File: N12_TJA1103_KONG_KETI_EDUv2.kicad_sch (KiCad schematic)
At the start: 65 parts, among them IC1 TJA1103AHN, J1 Conn_02x02_Odd_Even, J2 Conn_02x11_Odd_Even, J3 9-2304372-9, J4 E6S20A-40MT5-Z, Q1 FDN340P, Q2 BSS138, SW2 SW-DIP-ANGLED DS03-254-02BE, Y1 Crystal_GND24_Small

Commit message: fix: add E6S20A component library to assignment
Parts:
- J4: footprint YK_Footprint_LIB:E6S20A40MT5Z -> E6S20A:E6S20A40MT5Z
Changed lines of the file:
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@@
 			)
 		)
-		(property "Footprint" "YK_Footprint_LIB:E6S20A40MT5Z"
+		(property "Footprint" "E6S20A:E6S20A40MT5Z"
 			(at 154.94 191.44 0)
 			(effects

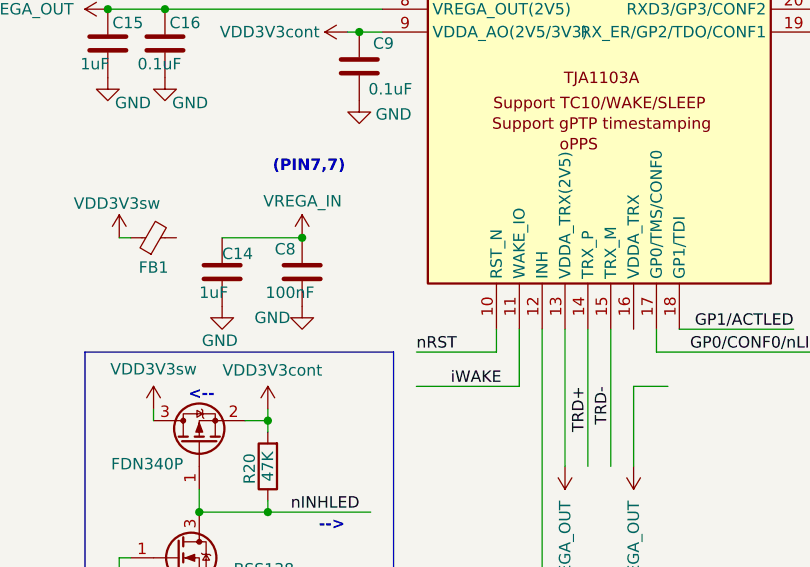
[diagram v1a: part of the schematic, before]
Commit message: fix: connect missing regulator and PHY supply pins
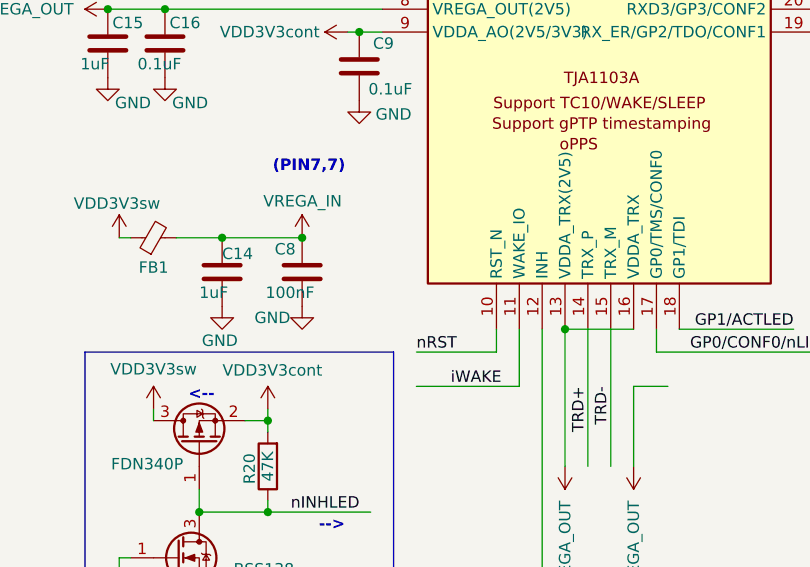
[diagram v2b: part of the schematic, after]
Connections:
- net VREGA_IN: now also FB1.2
- net VREGA_OUT: now also IC1.16 (VDDA_TRX)
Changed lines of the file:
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@@
 		)
+	)
+	(wire
+		(pts
+			(xy 29.21 92.71) (xy 34.29 92.71)
+		)
+		(stroke
+			(width 0)
+			(type default)
+		)
+	)
+	(junction
+		(at 34.29 92.71)
+		(diameter 0)
+		(color 0 0 0 0)
+	)
+	(wire
+		(pts
+			(xy 72.39 102.87) (xy 80.01 102.87)
+		)
+		(stroke
+			(width 0)
+			(type default)
+		)
+	)
+	(junction
+		(at 72.39 102.87)
+		(diameter 0)
+		(color 0 0 0 0)
 	)
 	(sheet_instances

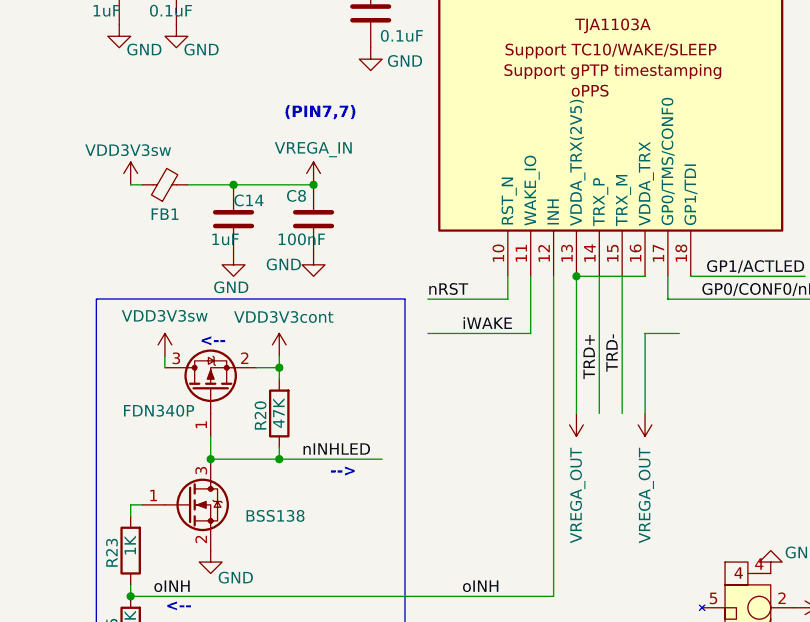
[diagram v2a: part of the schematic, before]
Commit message: fix: mark regulator rails as powered nets
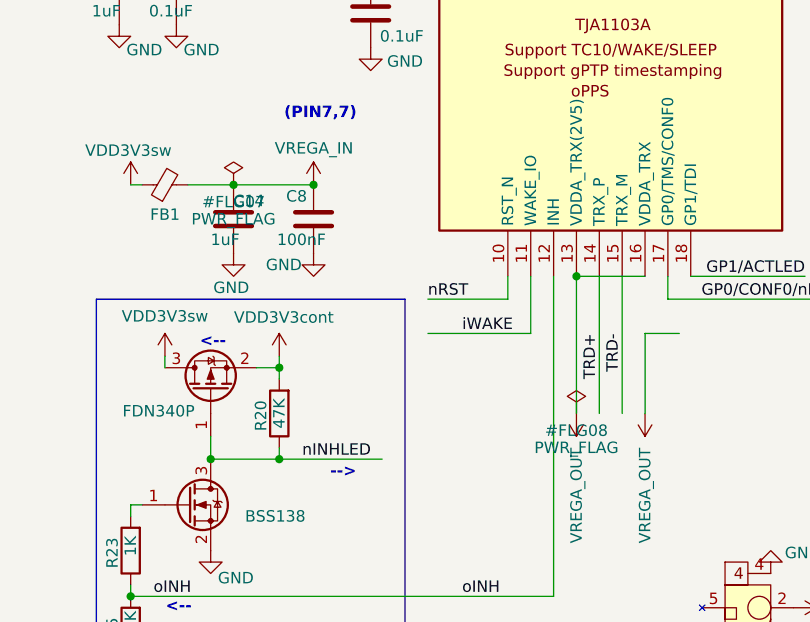
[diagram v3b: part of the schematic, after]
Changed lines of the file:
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@@
 		(color 0 0 0 0)
 	)
-	(sheet_instances
+    (symbol (lib_id "power:PWR_FLAG") (at 72.39 118.11 0) (unit 1)
+    (body_style 1) (exclude_from_sim no) (in_bom yes) (on_board yes) (in_pos_files yes) (dnp no)
+    (property "Reference" "#FLG08"
+      (at 72.39 120.015 0)
+      (show_name no)
+      (do_not_autoplace no)
+      (effects
+					(font
+						(size 1.27 1.27)
+					)
+				)
+    )
+    (property "Value" "PWR_FLAG"
+      (at 72.39 121.92 0)
+      (show_name no)
+      (do_not_autoplace no)
+      (effects
+					(font
+						(size 1.27 1.27)
+					)
+				)
+    )
+    (property "Footprint" ""
+      (at 72.39 118.11 0)
+      (hide yes)
+      (show_name no)
+      (do_not_autoplace no)
+      (effects
+					(font
+						(size 1.27 1.27)
+					)
+				)
+    )
+    (property "Datasheet" ""
+      (at 72.39 118.11 0)
+      (hide yes)
+      (show_name no)
+      (do_not_autoplace no)
+      (effects
+					(font
+						(size 1.27 1.27)
+					)
+				)
+    )
+    (property "Description" "Special symbol for telling ERC where power comes from"
+      (at 72.39 118.11 0)
+      (hide yes)
+      (show_name no)
+      (do_not_autoplace no)
+      (effects
+					(font
+						(size 1.27 1.27)
+					)
+				)
+    )
+    (pin "1")
+    (instances
+      (project "N12_TJA1103_KONG_KETI_EDUv2"
+        (path "/f2cee9b5-13fd-48f2-8e8c-2b940fa32210"
+          (reference "#FLG08")
+          (unit 1)
+        )
+      )
+    )
+  )
+    (symbol (lib_id "power:PWR_FLAG") (at 34.29 92.71 0) (unit 1)
+    (body_style 1) (exclude_from_sim no) (in_bom yes) (on_board yes) (in_pos_files yes) (dnp no)
+    (property "Reference" "#FLG07"
+      (at 34.29 94.615 0)
+      (show_name no)
+      (do_not_autoplace no)
+      (effects
+					(font
+						(size 1.27 1.27)
+					)
+				)
+    )
+    (property "Value" "PWR_FLAG"
+      (at 34.29 96.52 0)
+      (show_name no)
+      (do_not_autoplace no)
+      (effects
+					(font
+						(size 1.27 1.27)
+					)
+				)
+    )
+    (property "Footprint" ""
+      (at 34.29 92.71 0)
+      (hide yes)
+      (show_name no)
+      (do_not_autoplace no)
+      (effects
+					(font
+						(size 1.27 1.27)
+					)
+				)
+    )
+    (property "Datasheet" ""
+      (at 34.29 92.71 0)
+      (hide yes)
+      (show_name no)
+      (do_not_autoplace no)
+      (effects
+					(font
+						(size 1.27 1.27)
+					)
+				)
+    )
+    (property "Description" "Special symbol for telling ERC where power comes from"
+      (at 34.29 92.71 0)
+      (hide yes)
+      (show_name no)
+      (do_not_autoplace no)
+      (effects
+					(font
+						(size 1.27 1.27)
+					)
+				)
+    )
+    (pin "1")
+    (instances
+      (project "N12_TJA1103_KONG_KETI_EDUv2"
+        (path "/f2cee9b5-13fd-48f2-8e8c-2b940fa32210"
+          (reference "#FLG07")
+          (unit 1)
+        )
+      )
+    )
+  )
+  (sheet_instances
 		(path "/"
 			(page "1")

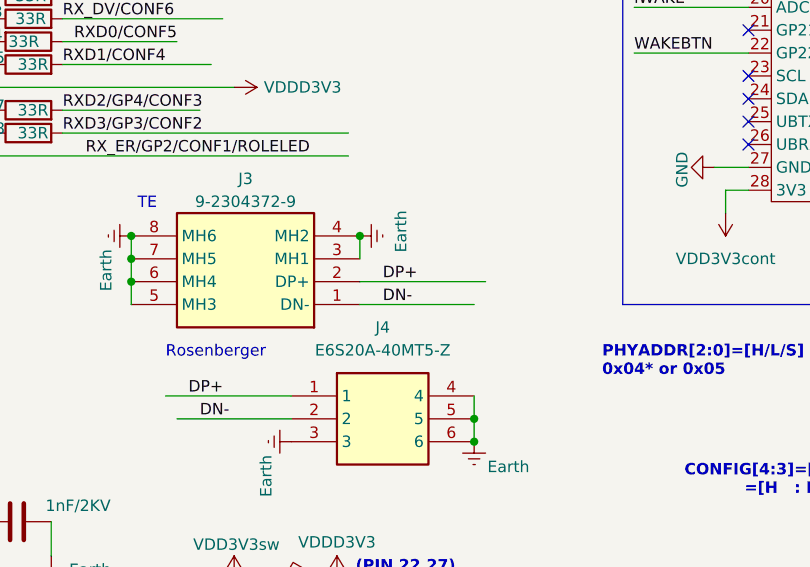
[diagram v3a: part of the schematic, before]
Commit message: fix: align schematic MATEnet polarity
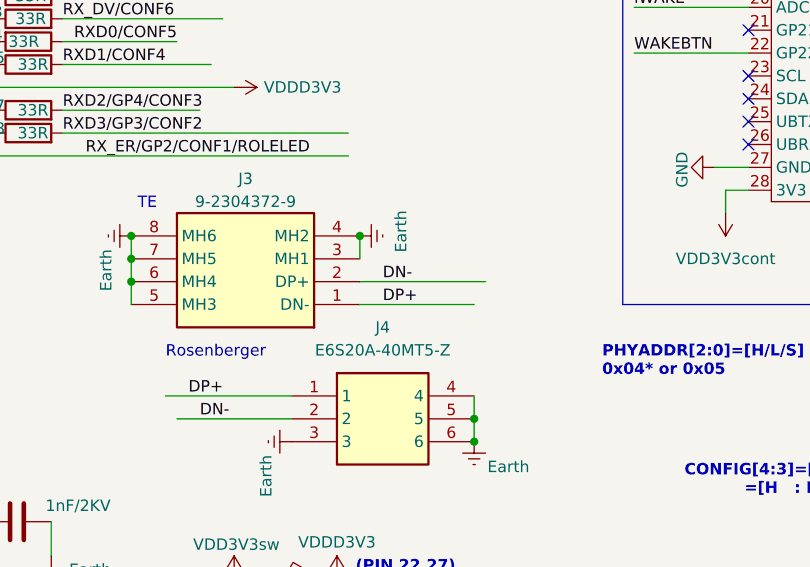
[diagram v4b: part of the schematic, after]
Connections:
- net DN-: now also J3.2 (DP+); no longer J3.1 (DN-)
- net DP+: now also J3.1 (DN-); no longer J3.2 (DP+)
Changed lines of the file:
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@@
 		)
 	)
-	(label "DN-"
+	(label "DP+"
 		(at 148.59 86.36 0)
 		(fields_autoplaced yes)
@@
 		)
 	)
-	(label "DP+"
+	(label "DN-"
 		(at 148.59 83.82 0)
 		(fields_autoplaced yes)
